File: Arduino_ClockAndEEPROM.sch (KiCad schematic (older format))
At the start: 13 parts, among them U1 24LC1025, U2 24LC1025, U3 DS1337S+, U4 ATmega328P-AU, Y1 Xtal 32MHz, Y2 Xtal 16MHz

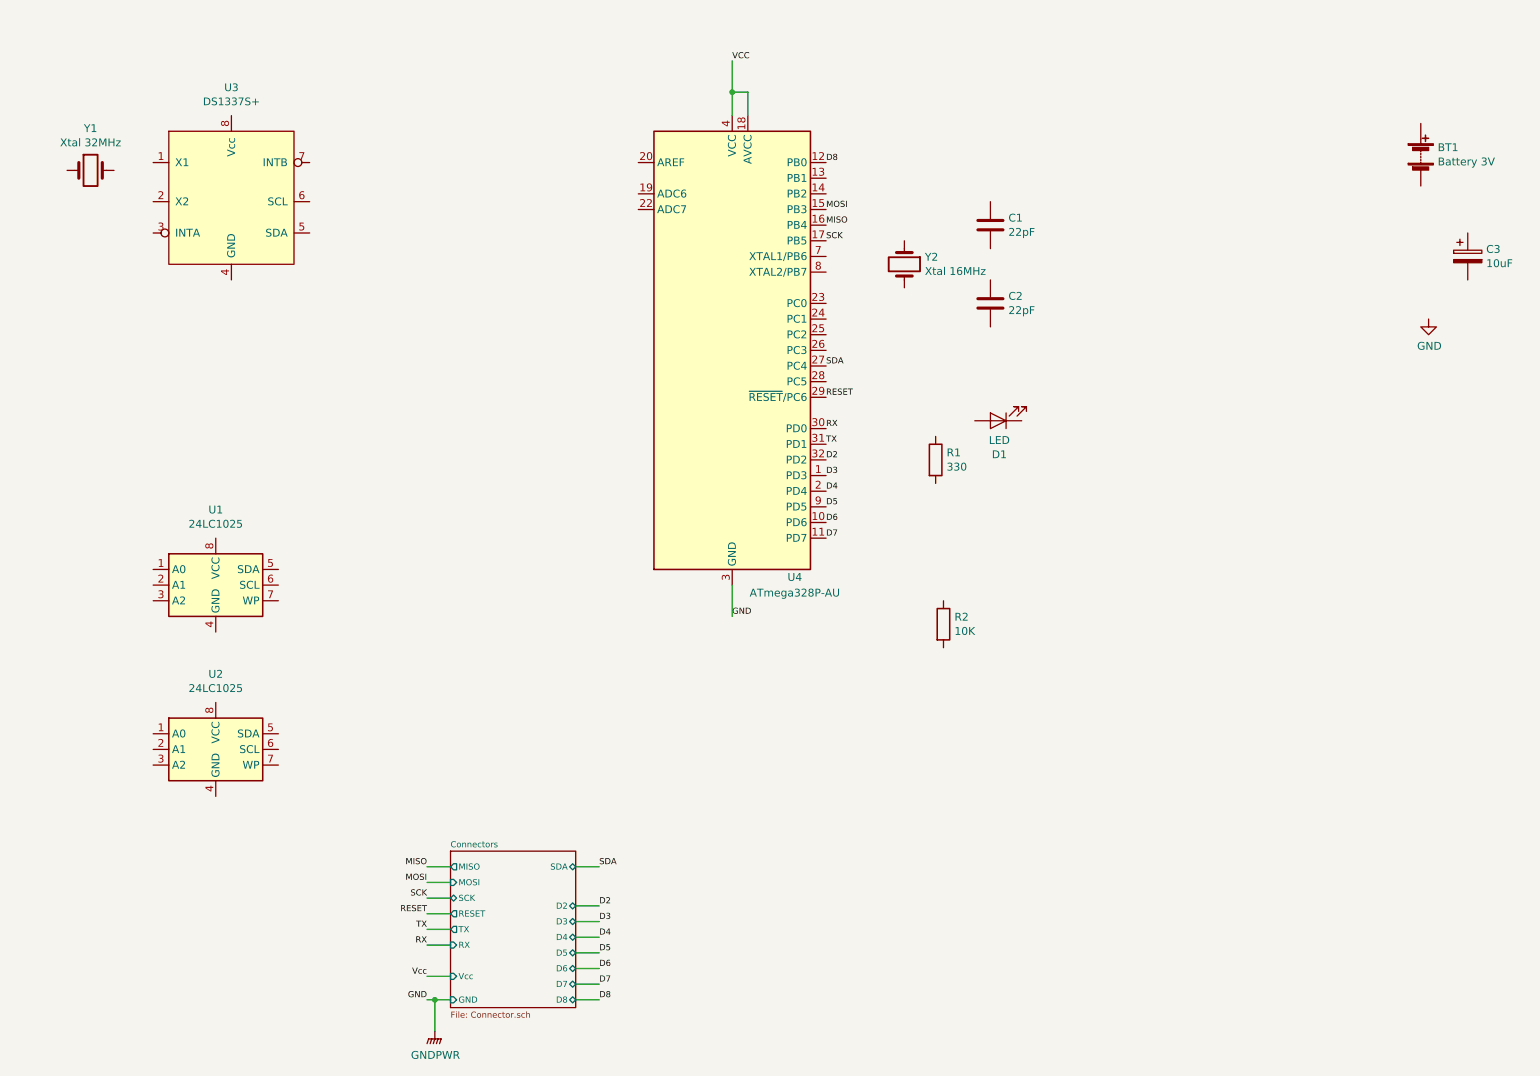
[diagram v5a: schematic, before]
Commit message: Completed wiring in all sheets.
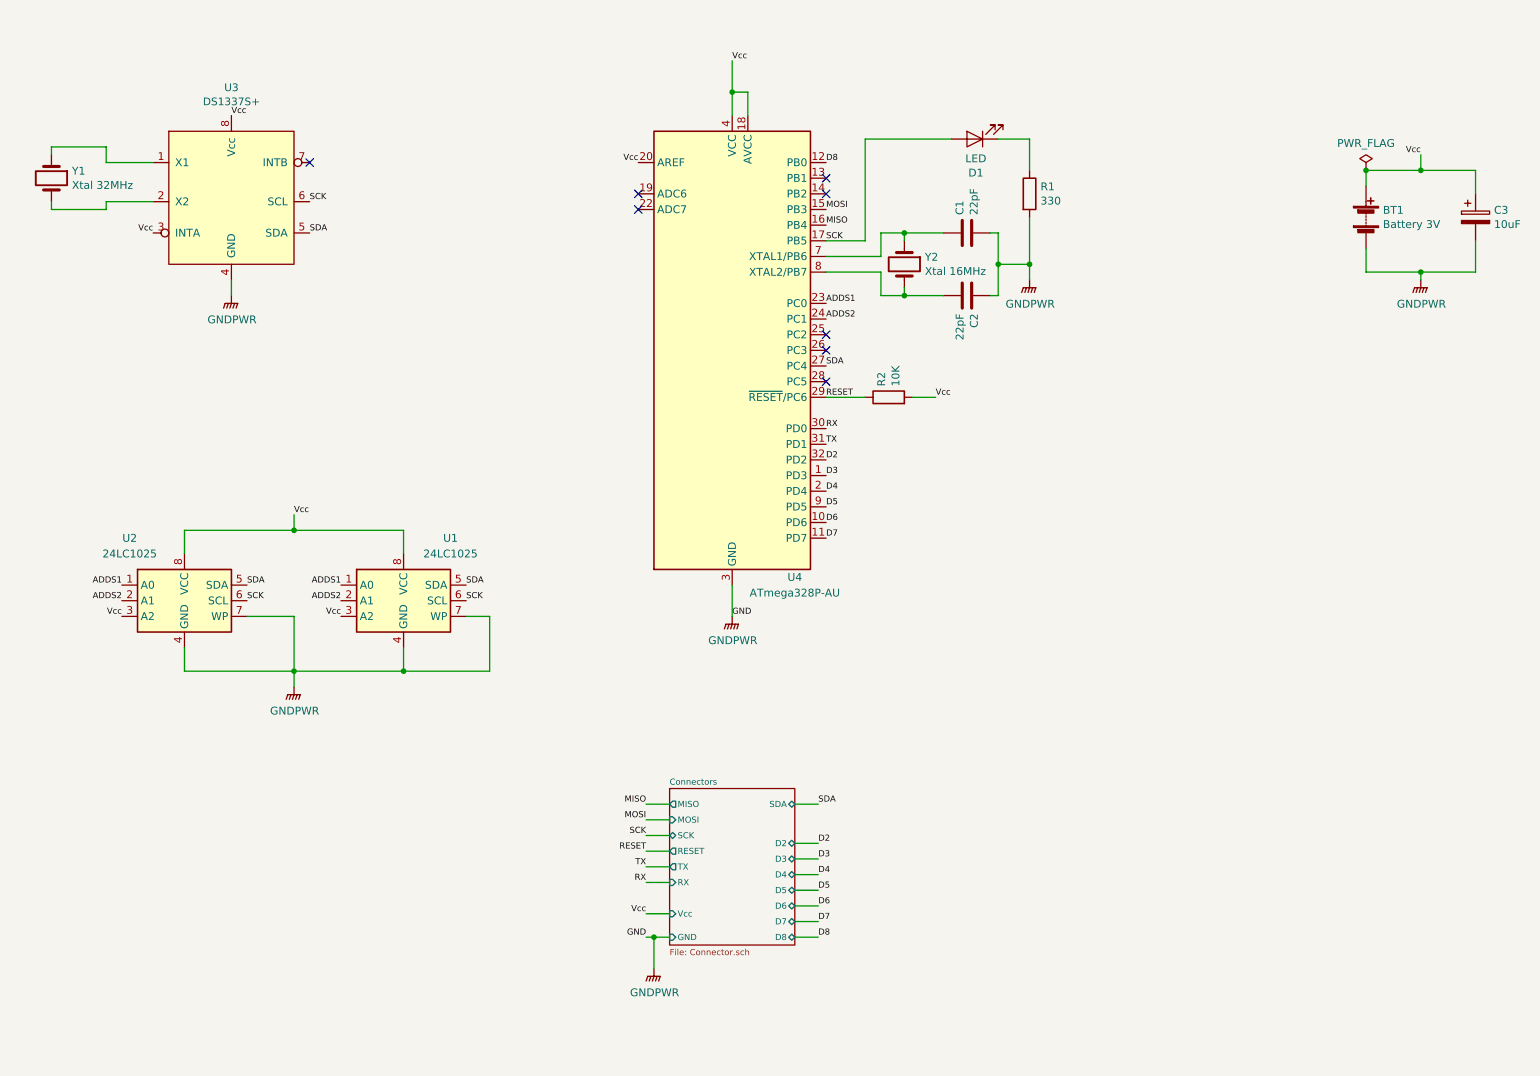
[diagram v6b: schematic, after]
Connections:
- net GND is gone; now on net GNDPWR: U4.21 (GND), U4.3 (GND), U4.5 (GND)
- net VCC is gone; now on net Vcc: U4.18 (AVCC), U4.4 (VCC), U4.6 (VCC)
- net RESET: now also R2.1
- net SCK: now also D1.2 (A), U1.6 (SCL), U2.6 (SCL), U3.6 (SCL)
- net SDA: now also U1.5 (SDA), U2.5 (SDA), U3.5 (SDA)
- net Vcc: now also BT1.1 (+), C3.1, R2.2, U1.3 (A2), U1.8 (VCC), U2.3 (A2), U2.8 (VCC), U3.3 (INTA), U3.8 (Vcc), U4.20 (AREF)
- net GNDPWR: now reaches BT1.2 (-)
- net GNDPWR: now also C1.2, C2.1, C3.2, R1.2, U1.4 (GND), U1.7 (WP), U2.4 (GND), U2.7 (WP), U3.4 (GND)
- net at C1.1: now also U4.7 (XTAL1/PB6), Y2.1
- net at C2.2: now also U4.8 (XTAL2/PB7), Y2.2
- net at D1.1 (K): now also R1.1
- net ADDS1: now reaches U1.1 (A0)
- net ADDS1: now also U2.1 (A0), U4.23 (PC0)
- net ADDS2: now reaches U1.2 (A1)
- net ADDS2: now also U2.2 (A1), U4.24 (PC1)
- net at U3.1 (X1): now also Y1.1
- net at U3.2 (X2): now also Y1.2
- no-connect marks 0 -> 8
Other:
- moved on the sheet: BT1, C1, C2, C3, D1, R1, R2, U1, U2, Y1

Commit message: Added functional block descriptions.
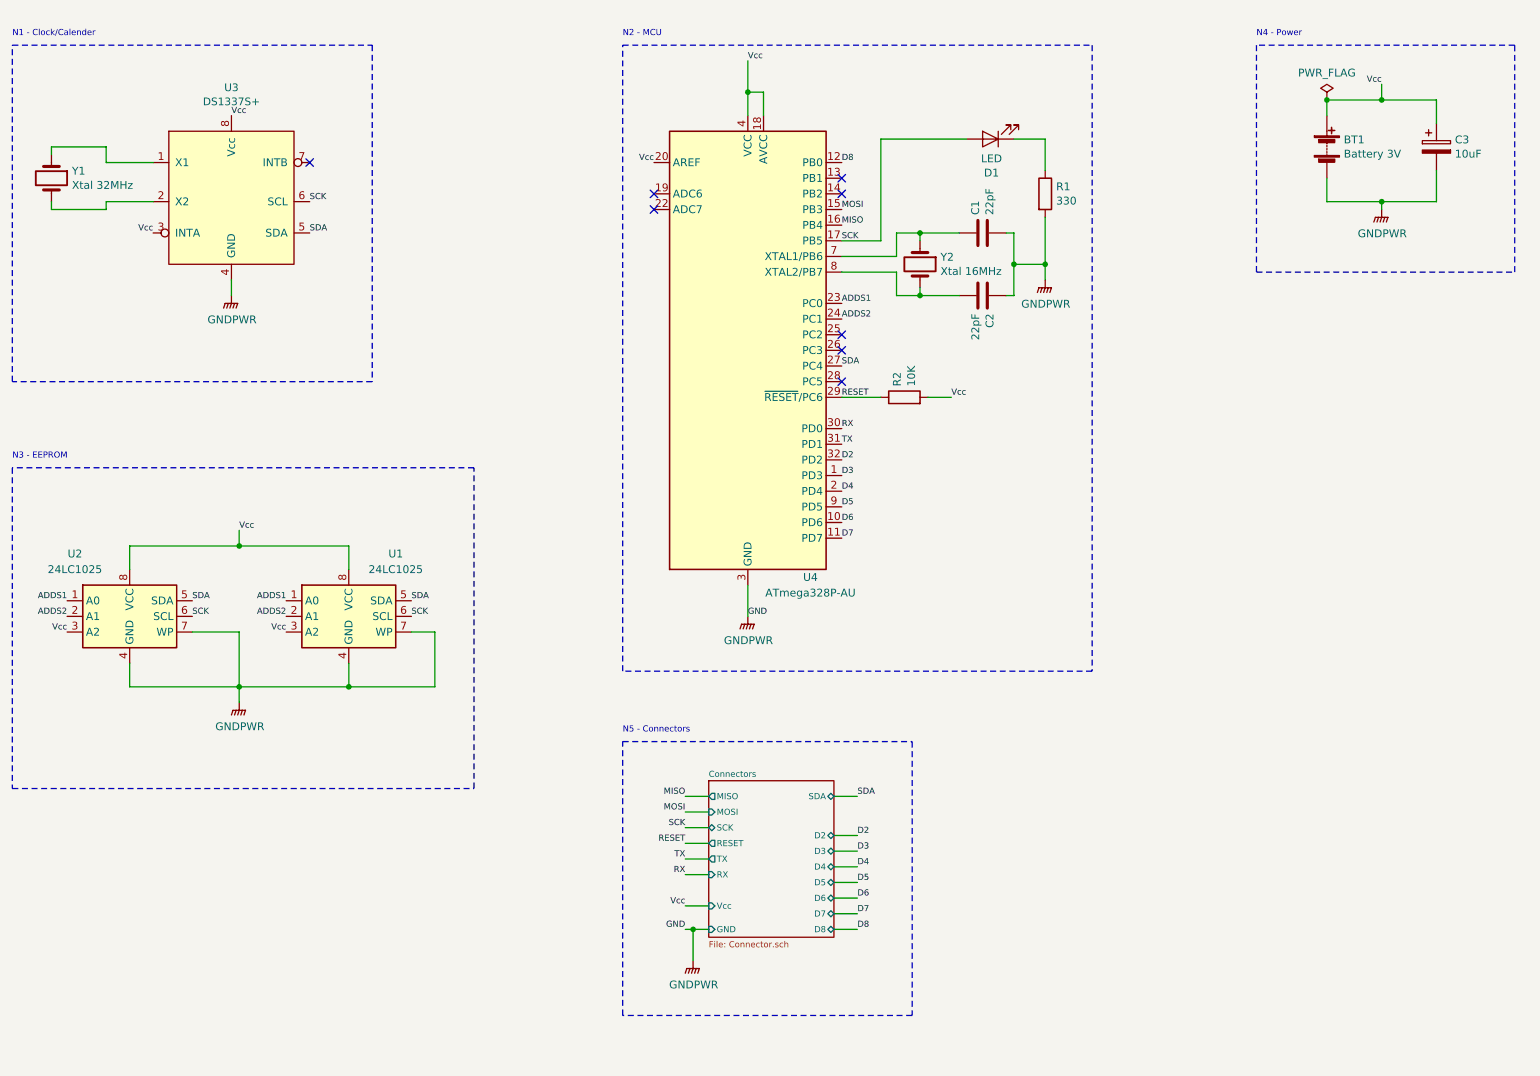
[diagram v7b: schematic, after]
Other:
- note added: "N1 - Clock/Calender"
- note added: "N2 - MCU"
- note added: "N3 - EEPROM"
- note added: "N4 - Power"
- note added: "N5 - Connectors"
- moved on the sheet: BT1, C1, C2, C3, D1, R1, R2, U1, U2, U4, Y2
